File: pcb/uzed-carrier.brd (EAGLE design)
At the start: 100 x 80 mm, 11 parts

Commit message: finished with uZed carrier board.
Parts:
- removed J1, J2: (no value), SparkFun-Connectors:1X08_ROUND
- removed J3: (no value), SparkFun-Connectors:1X06
- added 2V5_POWER: (no value), SparkFun-Connectors:1X06
- added 3V3_POWER/SPI, EXPOSURE_CTRL: (no value), SparkFun-Connectors:1X08_ROUND
- added C1: 10uF, SparkFun-Capacitors:EIA3216
- added SJ1, SJ3: (no value), SparkFun-Retired:SJ_3
- added UZEDLOWER, UZEDUPPER: (no value), SparkFun-Connectors:2X8
- moved 2V5_6 48.1 mm to (7.37, 37.1), flipped to the bottom, turned to 0 degrees
- moved 2V5_8 41.7 mm to (20.8, 30.7), flipped to the bottom, turned to 180 degrees
- moved 3V3_4 40.1 mm to (14.7, 13.2), flipped to the bottom, turned to 90 degrees
- moved 2V5_7 38.5 mm to (14.0, 30.7), flipped to the bottom, turned to 180 degrees
- moved 3V3_3 34.2 mm to (14.7, 20.8), flipped to the bottom, turned to 90 degrees
- moved 2V5_10 33.1 mm to (32.5, 38.6), flipped to the bottom
- moved IMAGE_DATA 25.5 mm to (35.6, 10.2), turned to 90 degrees
- moved 2V5_9 23.1 mm to (27.7, 30.7), flipped to the bottom, turned to 180 degrees
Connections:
- net CLK: now also EXPOSURE_CTRL.8, UZEDUPPER.15; no longer J2.8
- net D0: now also UZEDUPPER.12
- net D1: now also UZEDUPPER.11
- net D2: now also UZEDUPPER.10
- net D3: now also UZEDUPPER.9
- net D4: now also UZEDUPPER.8
- net D5: now also UZEDUPPER.7
- net D6: now also UZEDUPPER.6
- net D7: now also UZEDUPPER.5
- net D8: now also UZEDUPPER.4
- net D9: now also UZEDUPPER.3
- net FRAME_VALID: now also EXPOSURE_CTRL.2, UZEDLOWER.10; no longer J2.2
- net GND: now also 2V5_POWER.1, 3V3_POWER/SPI.5, C1.-, EXPOSURE_CTRL.6, SJ1.3, SJ3.3, UZEDUPPER.1, UZEDUPPER.2; no longer J1.5, J2.6, J3.1
- net INT_TIME1: now also EXPOSURE_CTRL.5, UZEDLOWER.11; no longer J2.5
- net INT_TIME2: now also EXPOSURE_CTRL.4, UZEDLOWER.13; no longer J2.4
- net INT_TIME3: now also EXPOSURE_CTRL.3, UZEDLOWER.15; no longer J2.3
- net LINE_VALID: now also EXPOSURE_CTRL.1, UZEDLOWER.9; no longer J2.1
- net RESET: now also EXPOSURE_CTRL.7, UZEDUPPER.16; no longer J2.7
- net SPI_CLK: now also 3V3_POWER/SPI.2, UZEDLOWER.3; no longer J1.2
- net SPI_DATA: now also 3V3_POWER/SPI.3, UZEDLOWER.5; no longer J1.3
- net SPI_EN: now also 3V3_POWER/SPI.1, UZEDLOWER.1; no longer J1.1
- net VADC: now also 2V5_POWER.4; no longer J3.4
- net VDDA: now also 2V5_POWER.5; no longer J3.5
- net VDDD: now also 2V5_POWER.3; no longer J3.3
- net VDDO: now also 2V5_POWER.2; no longer J3.2
- net VIN: now also C1.+, UZEDLOWER.7, UZEDLOWER.8
- net VMEM_H: now also 3V3_POWER/SPI.4; no longer J1.4
- net VPIX: now also 2V5_POWER.6; no longer J3.6
- net VRESET_1: now also 3V3_POWER/SPI.6, SJ1.1, SJ3.1; no longer J1.6
- net VRESET_2: now also 3V3_POWER/SPI.7, SJ1.2; no longer J1.7
- net VRESET_3: now also 3V3_POWER/SPI.8, SJ3.2; no longer J1.8
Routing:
- net VIN: track 0.00 -> 163.4 mm
- net SPI_DATA: track 0.00 -> 65.3 mm
- net SPI_CLK: track 0.00 -> 64.1 mm
- net SPI_EN: track 0.00 -> 62.9 mm
- net FRAME_VALID: track 0.00 -> 44.3 mm
- net LINE_VALID: track 0.00 -> 44.1 mm
- net RESET: track 0.00 -> 38.1 mm
- net INT_TIME3: track 0.00 -> 35.7 mm
- net INT_TIME1: track 0.00 -> 33.3 mm
- net INT_TIME2: track 0.00 -> 33.1 mm
- net VRESET_1: track 0.00 -> 32.3 mm
- net CLK: track 0.00 -> 32.1 mm
- net D0: track 0.00 -> 26.4 mm
- net D2: track 0.00 -> 24.2 mm
- net D1: track 0.00 -> 22.2 mm
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- added copper zone on layer 1, net GND
- added copper zone on layer 16, net GND
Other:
- board size 100 x 80 mm -> 53.5 x 43.2 mm
- board text added: "LUPA300 + uZED Matt Ruffner 2017 v1.0"

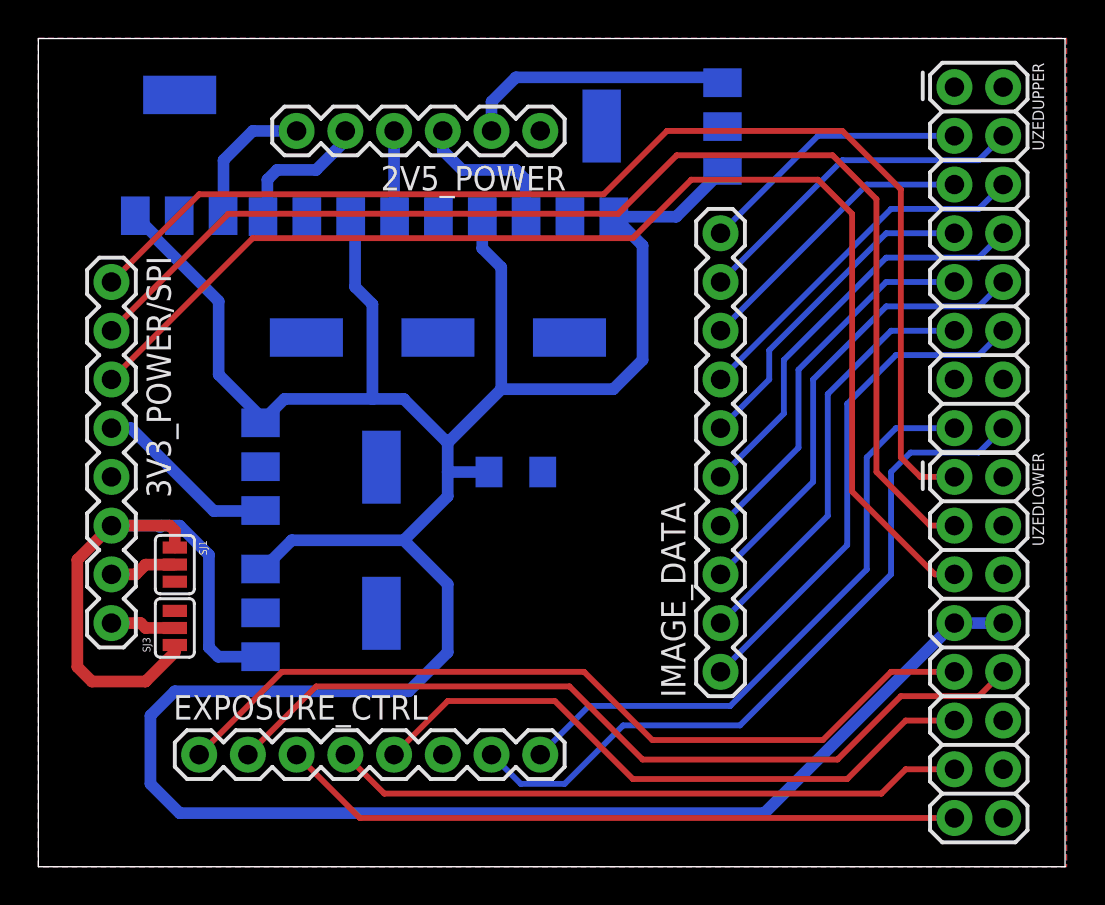
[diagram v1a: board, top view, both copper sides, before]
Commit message: made vias smaller and fixed silkscreen
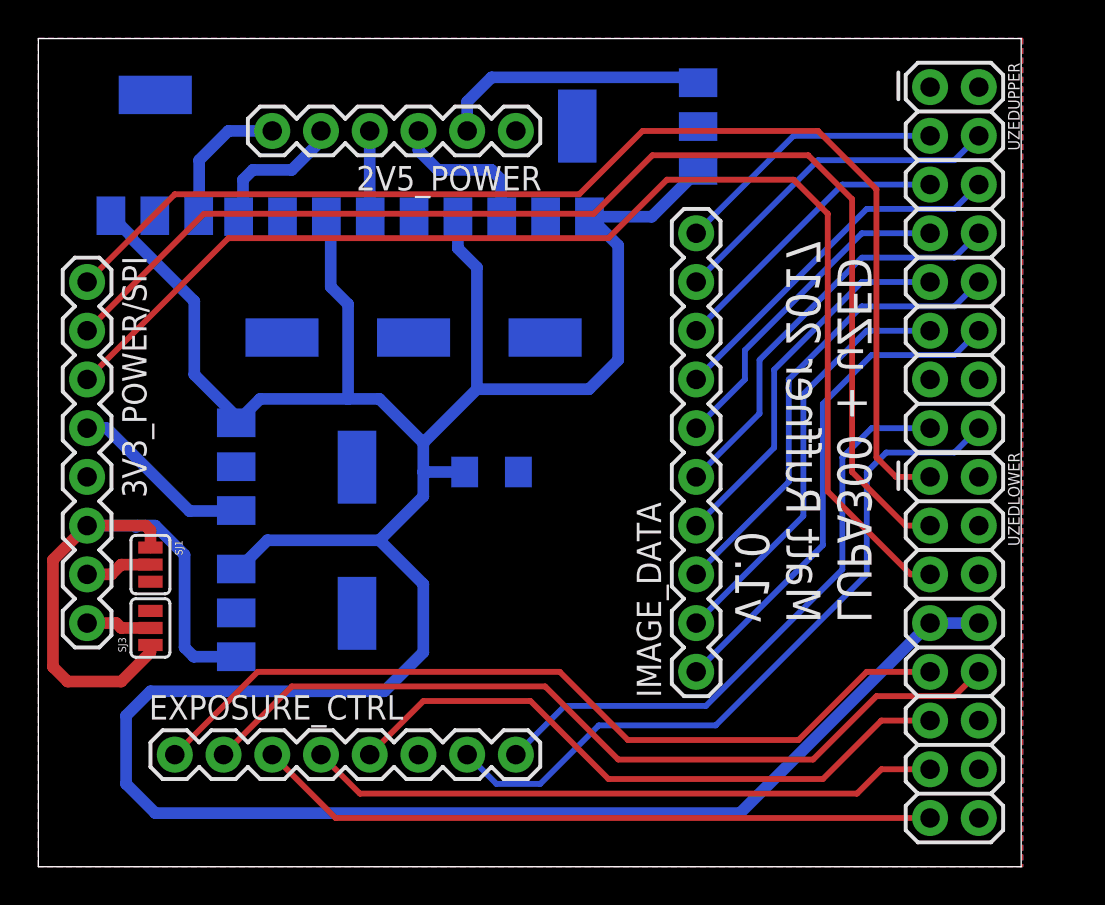
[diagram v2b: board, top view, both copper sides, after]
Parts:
- moved IMAGE_DATA 1.27 mm to (34.3, 10.2)
- moved UZEDLOWER 1.27 mm to (46.5, 20.3)
- moved UZEDUPPER 1.27 mm to (46.5, 40.6)
- moved 2V5_7 1.27 mm to (12.7, 30.7)
- moved SJ1 1.27 mm to (5.84, 15.7)
- moved SJ3 1.27 mm to (5.84, 12.4)
- moved 3V3_POWER/SPI 1.27 mm to (2.54, 30.5)
- moved 2V5_10 1.27 mm to (31.2, 38.6)
- moved 2V5_6 1.27 mm to (6.10, 37.1)
- moved 2V5_8 1.27 mm to (19.6, 30.7)
- moved 2V5_9 1.27 mm to (26.4, 30.7)
- moved 2V5_POWER 1.27 mm to (24.9, 38.4)
- moved 3V3_3 1.27 mm to (13.5, 20.8)
- moved 3V3_4 1.27 mm to (13.5, 13.2)
- moved C1 1.27 mm to (23.6, 20.6)
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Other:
- board size 53.5 x 43.2 mm -> 51.2 x 43.2 mm
